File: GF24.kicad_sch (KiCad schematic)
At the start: 34 parts, among them J1 Conn_02x05_Odd_Even, J2 USB_C_Receptacle_PowerOnly_6P, Q1 BC817-25LT1G, SW1 NRST, SW2 SW_Nidec_CAS-120A1, SW3 NRST, U1 STM32F031C4T6, U2 MAX-M10S, U3 LM3671MF-3.3, U4 LTC1733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

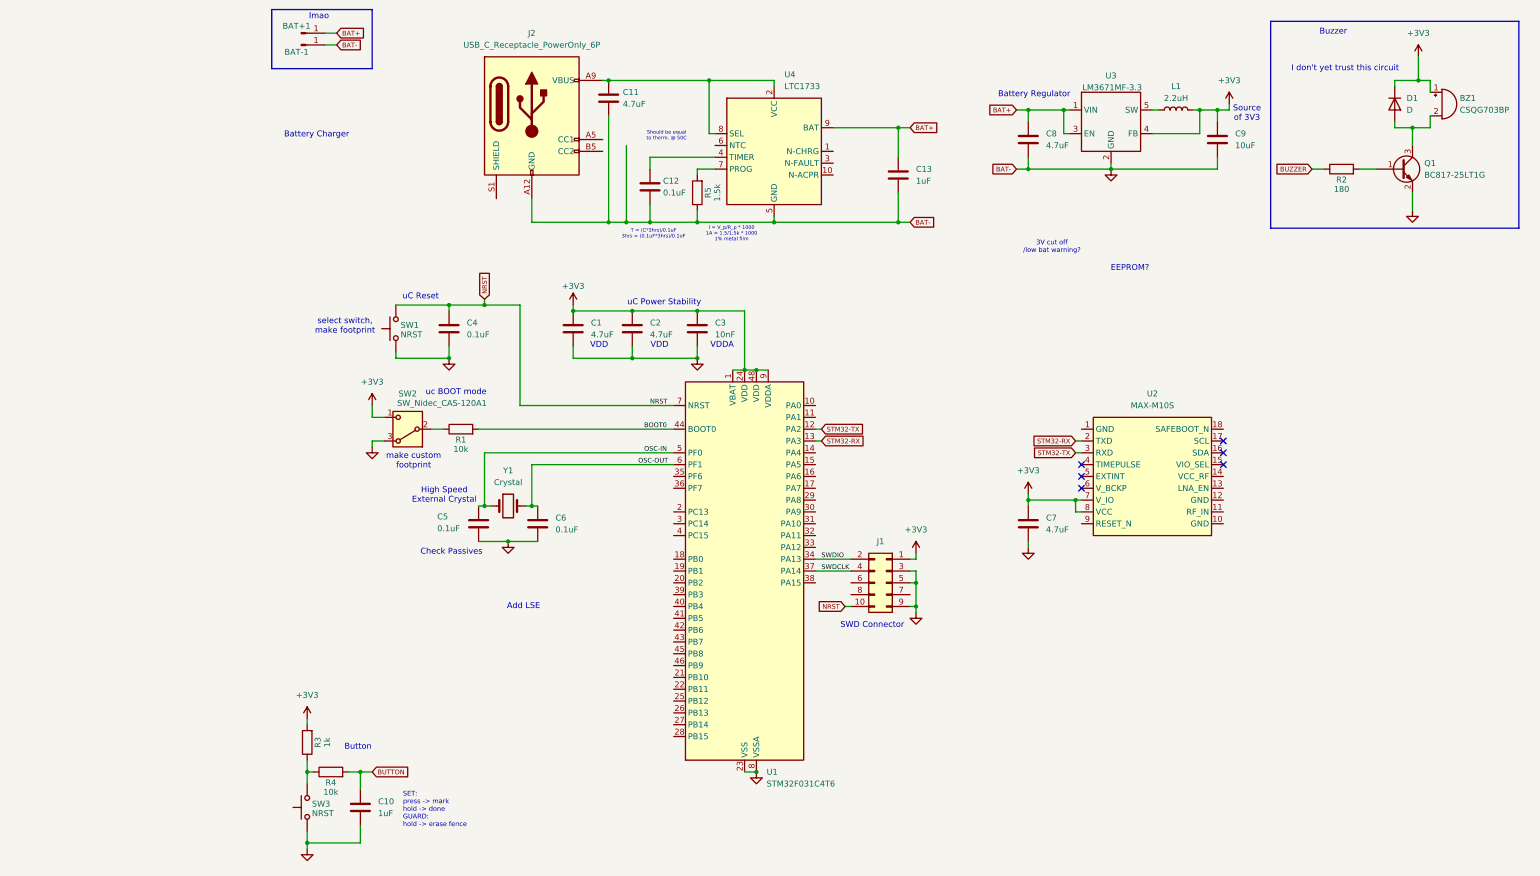
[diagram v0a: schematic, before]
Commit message: selected components for battery charger
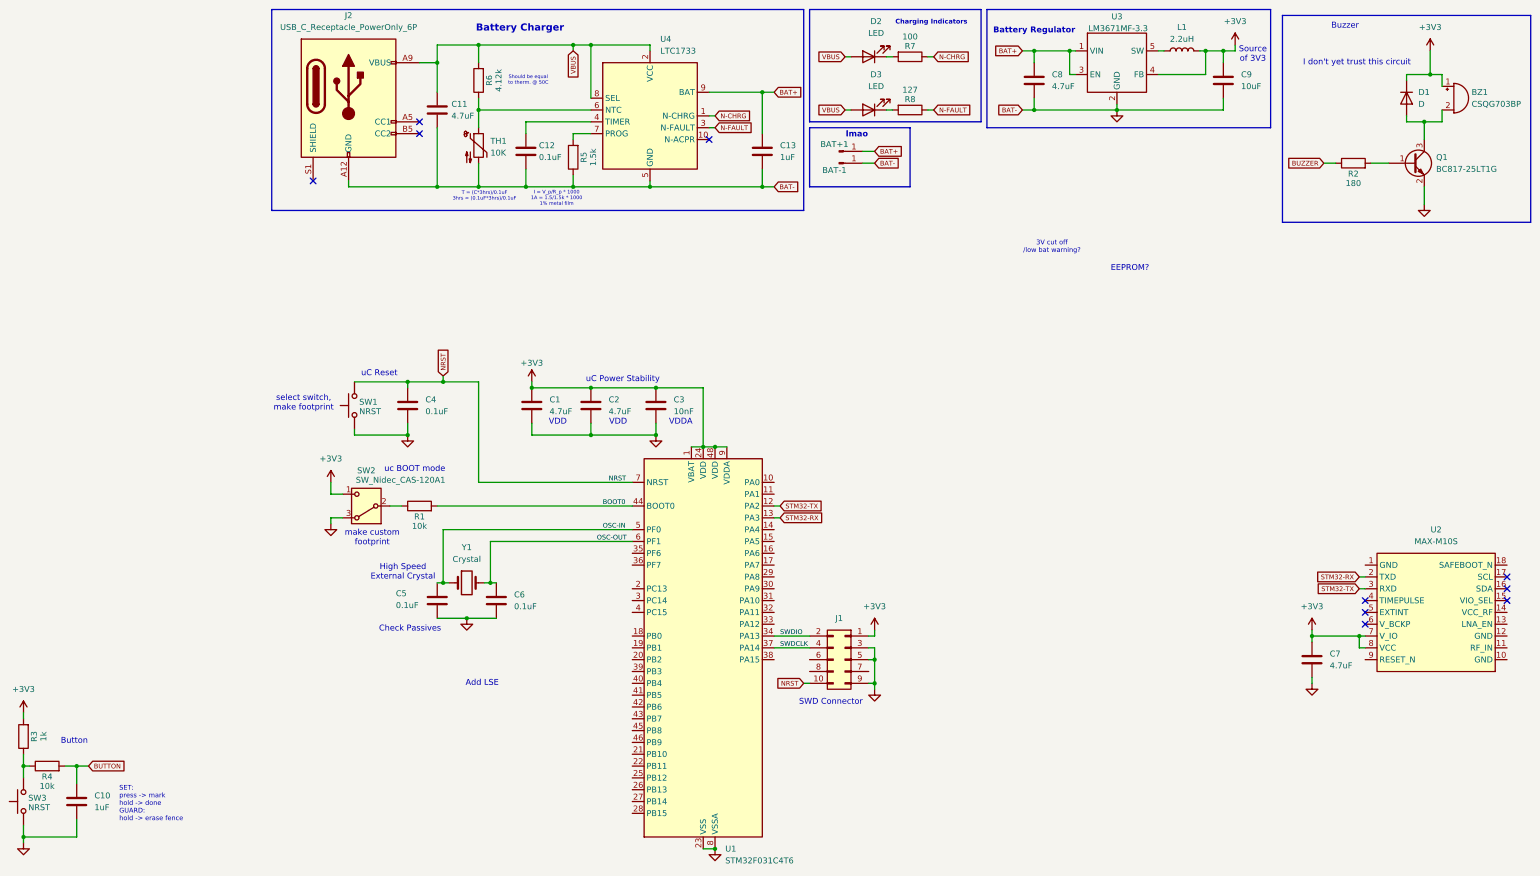
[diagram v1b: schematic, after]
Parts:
- added D2, D3: LED, symbol Device:LED
- added R6: 4.12k, MB-Generic:R1206_medium, symbol Device:R
- added R7: 100, MB-Generic:R1206_medium, symbol Device:R
- added R8: 127, MB-Generic:R1206_medium, symbol Device:R
- added TH1: 10K, symbol Device:Thermistor_NTC
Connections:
- net GND: now also TH1.2
- net N-CHRG: now reaches U4.1 (N-CHRG)
- net N-CHRG: now also R7.1
- net VBUS: now reaches C11.1, J2.A9 (VBUS), J2.B9 (VBUS), U4.2 (VCC), U4.8 (SEL)
- net VBUS: now also D2.2 (A), D3.2 (A), R6.2
- net N-FAULT: now reaches U4.3 (N-FAULT)
- net N-FAULT: now also R8.1
- net at U4.6 (NTC): now also R6.1, TH1.1
- new net: D2.1 (K), R7.2
- new net: D3.1 (K), R8.2
- no-connect marks 6 -> 10
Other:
- note added: "Charging Indicators"
- moved on the sheet: BAT+1, BAT-1, BZ1, C1, C10, C11, C12, C13, C2, C3, C4, C5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

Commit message: updated battery regulator circuit. oof
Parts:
- removed L1: 2.2uH, MB-Generic:PCC-M0530M-H, symbol Device:L
- removed U3: LM3671MF-3.3, MB-SOT:SOT-23-5, symbol MB-V-REG:LM3671
- added D4: LED, symbol Device:LED
- added R10: 47, MB-Generic:R1206_medium, symbol Device:R
- added R9: 47k, MB-Generic:R1206_medium, symbol Device:R
- added SW4: ON/OFF, symbol Switch:SW_SPST
- added U3: TPS745, symbol MB-V-REG:TPS74533PQWDRVRQ1
- C8: value 4.7uF -> 1uF
- C9: value 10uF -> 1uF
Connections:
- net +3V3: now also R9.2, U3.1 (OUT)
- net BAT+: now also D4.2 (A), SW4.1 (A); no longer C8.1
- net GND: now also U3.3 (GND)
- new net: D4.1 (K), R10.2
- new net: C8.1, SW4.2 (B), U3.4 (EN), U3.6 (IN)
- new net PG: R10.1, R9.1, U3.5 (PG)
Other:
- note added: "Add LSE?"
- note added: "Low Battery Indicator"
- note added: "Mode Switch"
- note added: "PG is open drain when power is not good (lmao)"
- note removed: "3V cut off /low bat warning?"
- note removed: "Add LSE"
- moved on the sheet: BZ1, C10, C8, C9, D1, Q1, R2, R3, R4, SW3

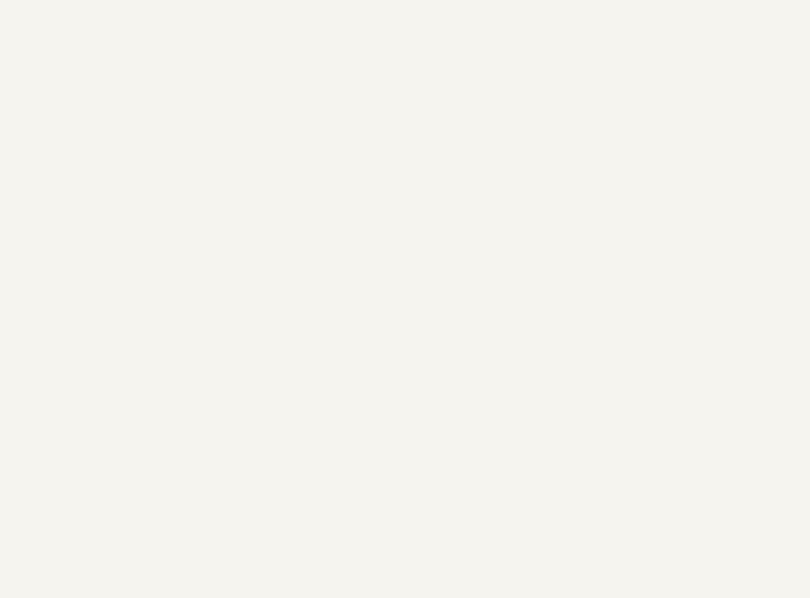
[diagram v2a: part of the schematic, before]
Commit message: started to add EEPROM
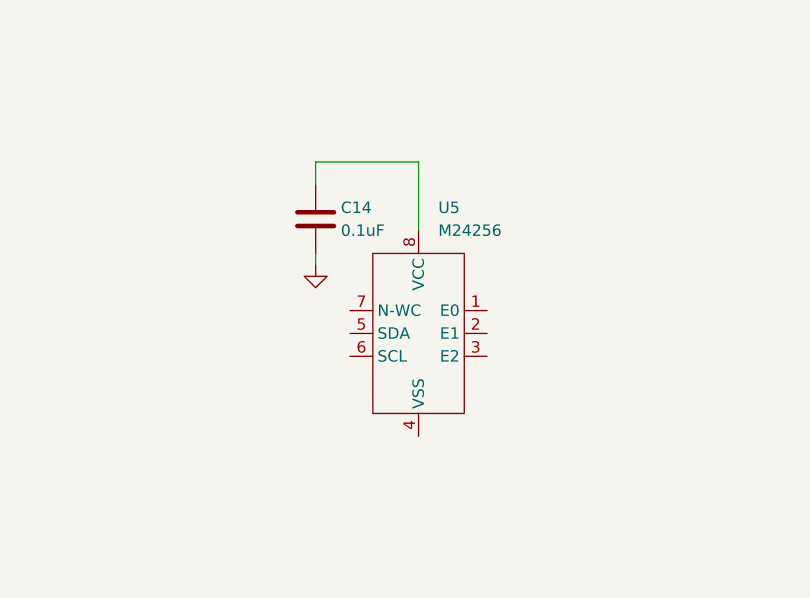
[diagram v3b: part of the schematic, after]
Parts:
- added C14: 0.1uF, MB-Generic:C1206_medium, symbol Device:C
- added U5: M24256, symbol MB-EEPROM:M24256-BFMC6TG
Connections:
- net GND: now also C14.2
- new net: C14.1, U5.8 (VCC)

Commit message: idk
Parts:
- added R11, R12: 4.7k, MB-Generic:R1206_medium, symbol Device:R
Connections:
- net +3V3: now also R11.2, R12.2
- net GND: now also U5.1 (E0), U5.2 (E1), U5.3 (E2), U5.4 (VSS)
- net SDA: now reaches U5.5 (SDA)
- net SDA: now also U1.22 (PB11), R12.1
- net SCL: now reaches U5.6 (SCL)
- net SCL: now also U1.21 (PB10), R11.1
- net EEPROM-N-WC: now reaches U5.7 (N-WC)
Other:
- note removed: "EEPROM?"

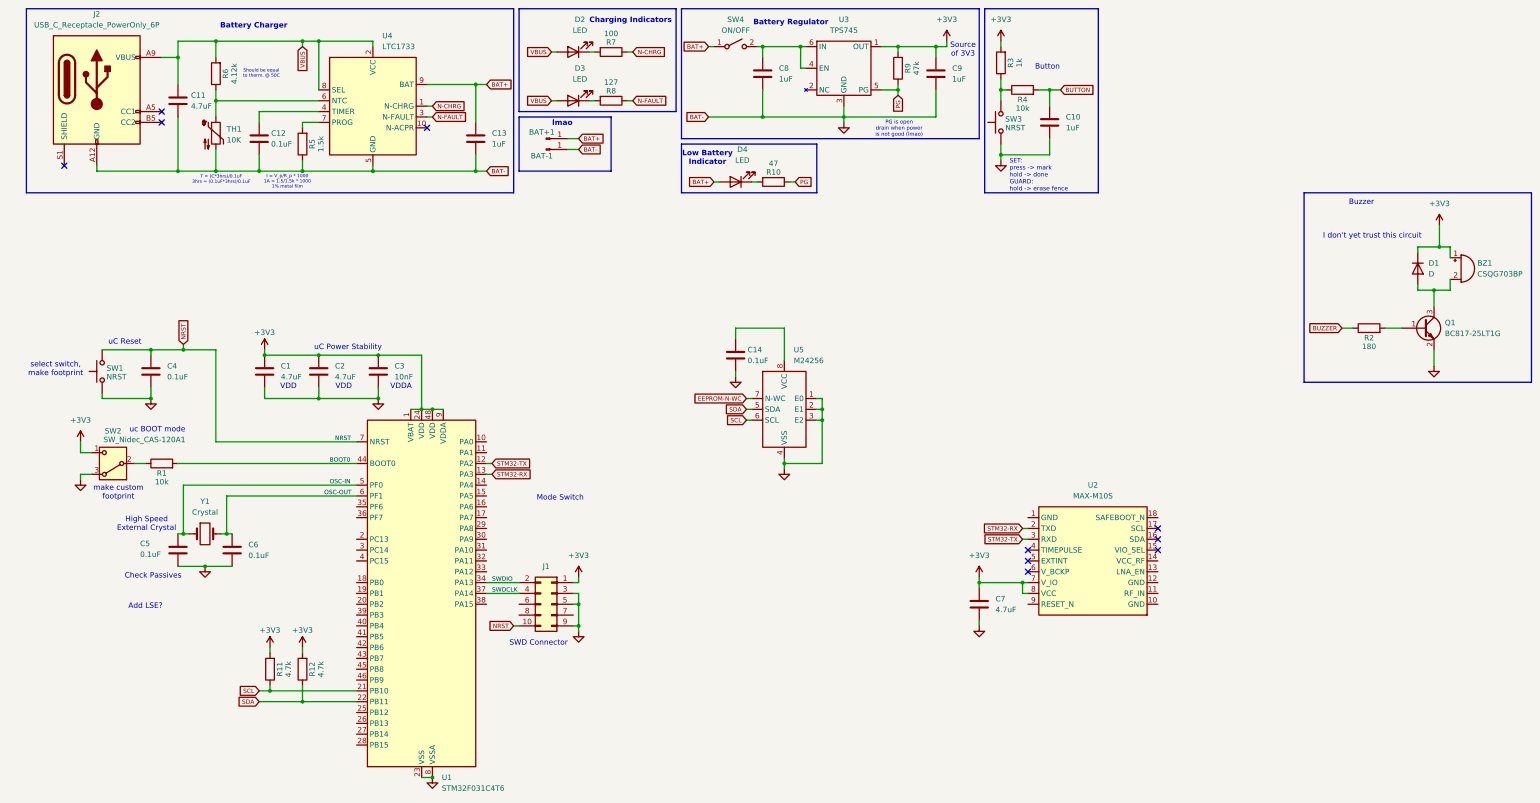
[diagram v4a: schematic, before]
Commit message: swapped GNSS again. Close to done with schematic
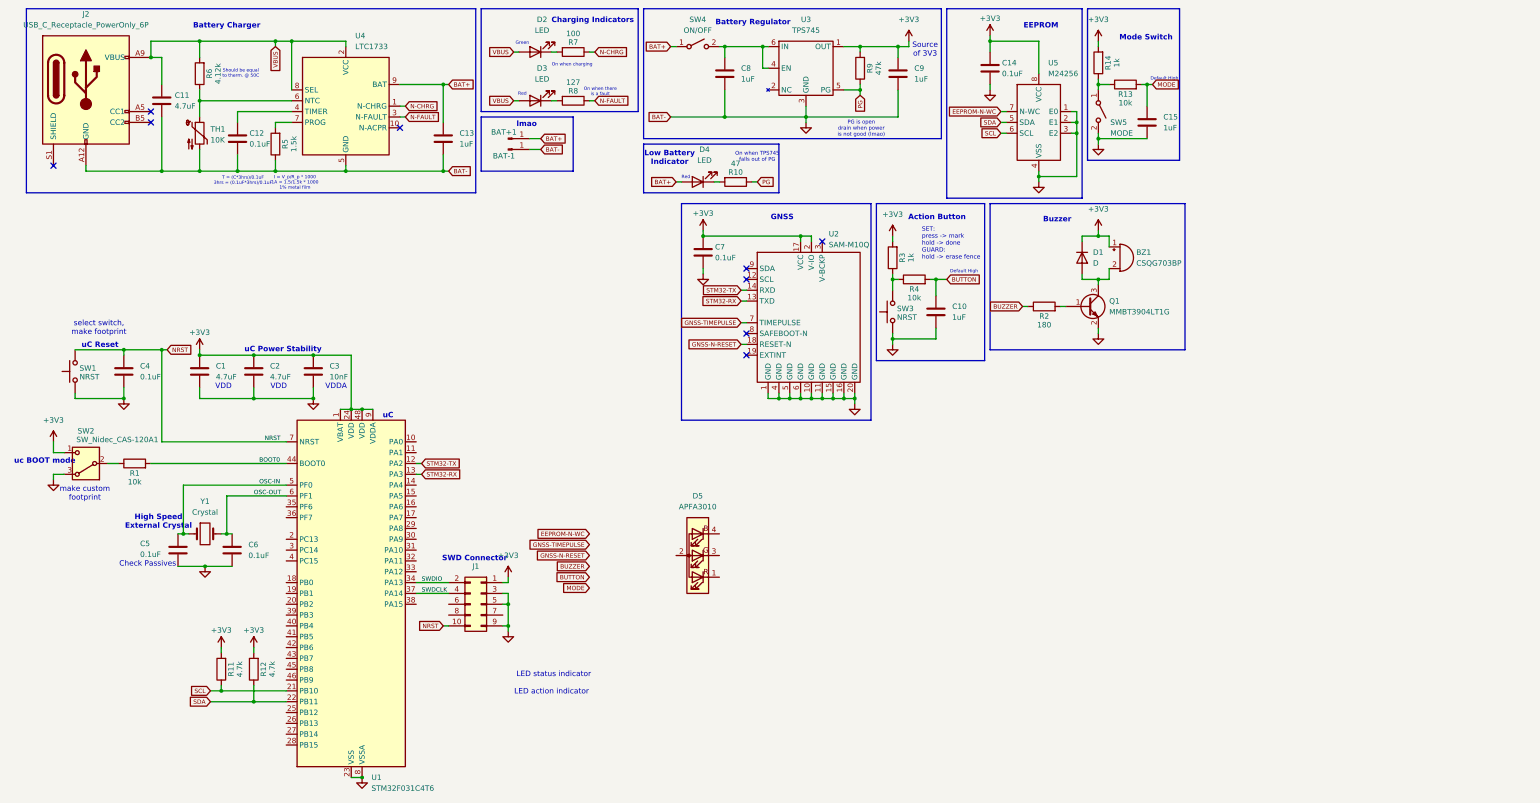
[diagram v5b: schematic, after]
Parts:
- removed U2: MAX-M10S, MB-GNSS:MAX-M10S, symbol MB-GNSS:MAX-M10S
- added C15: 1uF, MB-Generic:C1206_medium, symbol Device:C
- added D5: APFA3010, LED_SMD:LED_Kingbright_APFA3010_3x1.5mm_Horizontal, symbol LED:APFA3010
- added R13: 10k, MB-Generic:R1206_medium, symbol Device:R
- added R14: 1k, MB-Generic:R1206_medium, symbol Device:R
- added SW5: MODE, symbol Switch:SW_SPST
- added U2: SAM-M10Q, symbol MB-GNSS:SAM-M10Q
- C7: value 4.7uF -> 0.1uF
- Q1: value BC817-25LT1G -> MMBT3904LT1G
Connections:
- net +3V3: now also C14.1, U5.8 (VCC), R14.2, U2.17 (VCC), U2.2 (V-IO)
- net GND: now also C15.2, SW5.2 (B), U2.1 (GND), U2.10 (GND), U2.11 (GND), U2.15 (GND), U2.16 (GND), U2.20 (GND), U2.4 (GND), U2.5 (GND), U2.6 (GND)
- net STM32-RX: now also U2.13 (TXD)
- net STM32-TX: now also U2.14 (RXD)
- new net: R13.1, R14.1, SW5.1 (A)
- new net GNSS-N-RESET: U2.18 (RESET-N)
- new net GNSS-TIMEPULSE: U2.7 (TIMEPULSE)
- new net MODE: C15.1, R13.2
- no-connect marks 10 -> 9
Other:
- note added: "Action Button"
- note added: "Default High"
- note added: "EEPROM"
- note added: "GNSS"
- note added: "Green"
- note added: "LED action indicator"
- note added: "LED status indicator"
- note added: "On when TPS745 falls out of PG"
- note added: "On when charging"
- note added: "On when there is a fault"
- note added: "Red"
- note added: "uC"
- note removed: "Add LSE?"
- note removed: "Button"
- note removed: "I don't yet trust this circuit"
- moved on the sheet: BAT+1, BAT-1, BZ1, C1, C10, C11, C12, C13, C14, C2, C3, C4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
